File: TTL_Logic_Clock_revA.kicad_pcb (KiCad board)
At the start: 2 copper layers, 105.5 x 99.6 mm, 95 parts, among them J1 PJ-202A, J2 Conn_01x04_Female, U1 SN74HC74N, U10 SN74LS47N, U11 SN74LS190N, U12 SN74LS47N, U13 SN74LS47N, U14 SN74LS47N, U15 SN74LS47N, U2 SN74HC00N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

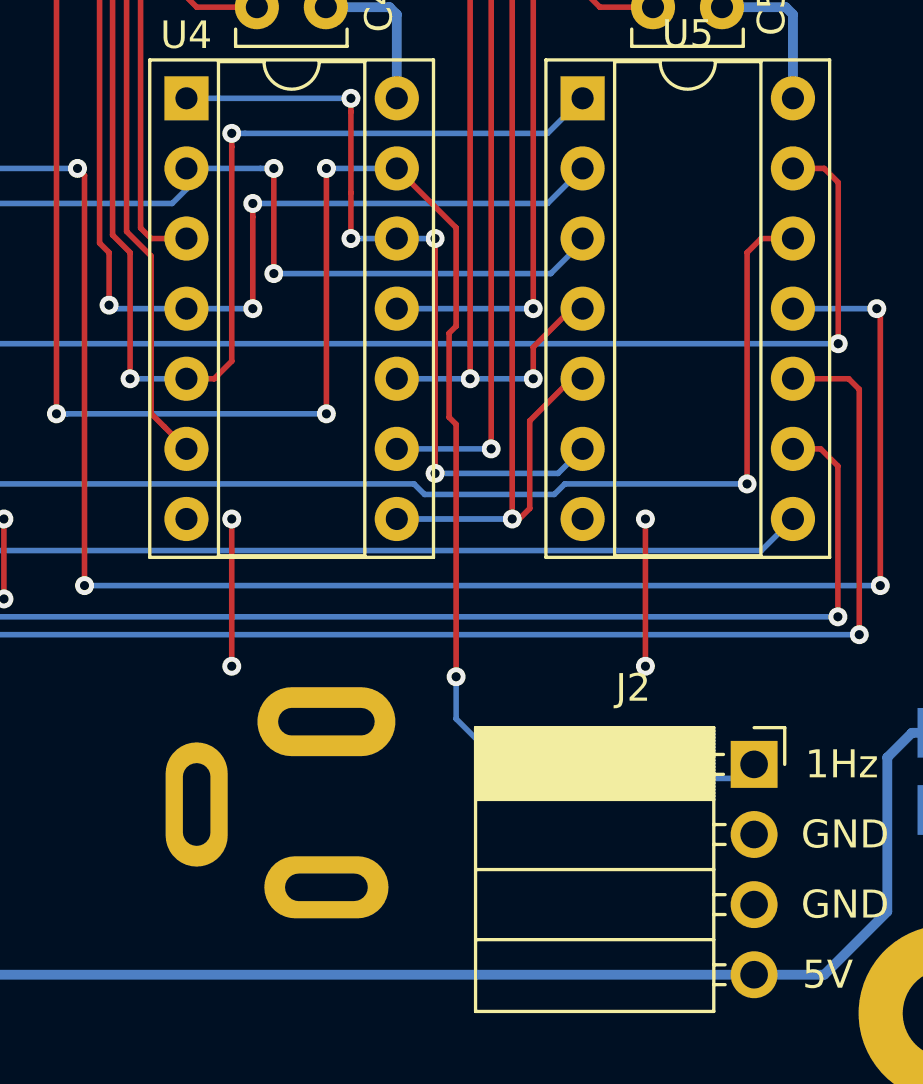
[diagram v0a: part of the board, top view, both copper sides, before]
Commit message: Revert "new updates"
This reverts commit 53f30aa524d5c5c52be93e0d1f9b706b91b0ddee.
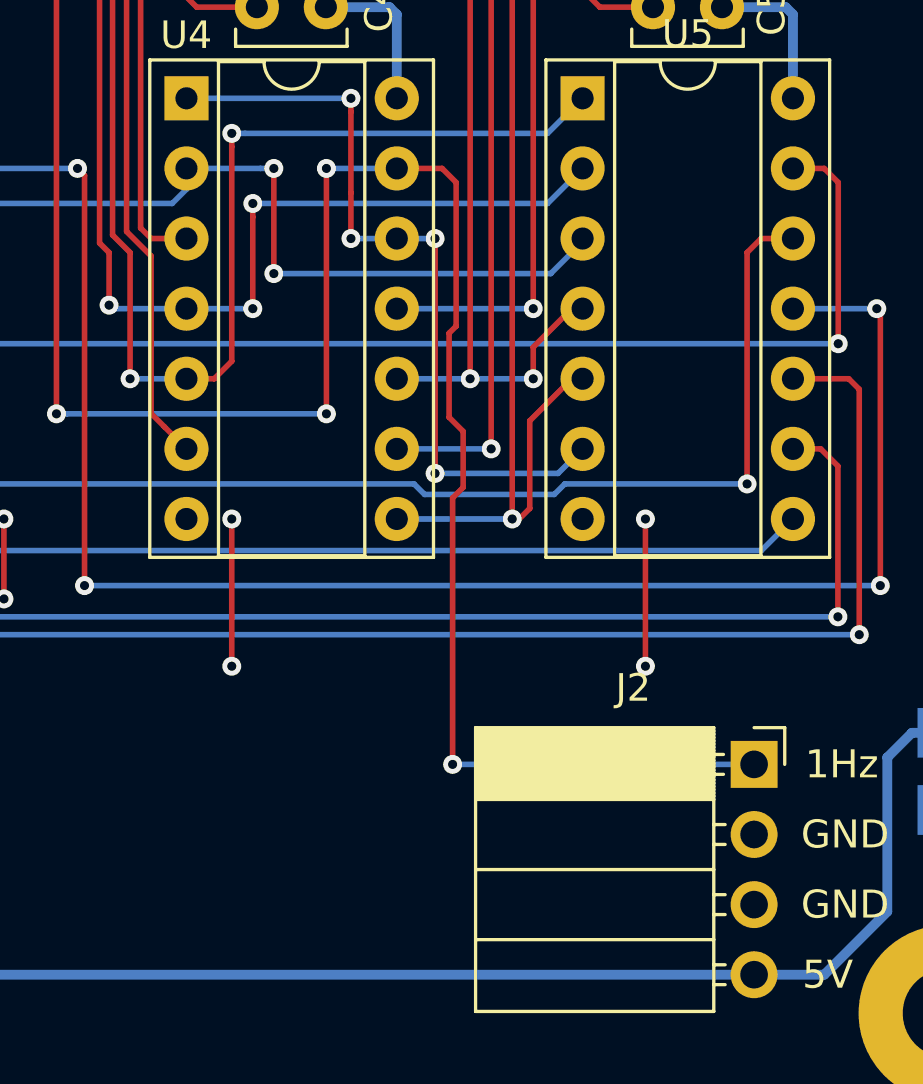
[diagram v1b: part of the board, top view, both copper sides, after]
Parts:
- removed J1: PJ-202A, harit-connectors-dc:CUI_PJ-202A
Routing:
- net 1Hz: track 183.2 -> 185.1 mm
